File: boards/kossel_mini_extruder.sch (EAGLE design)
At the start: 31 parts

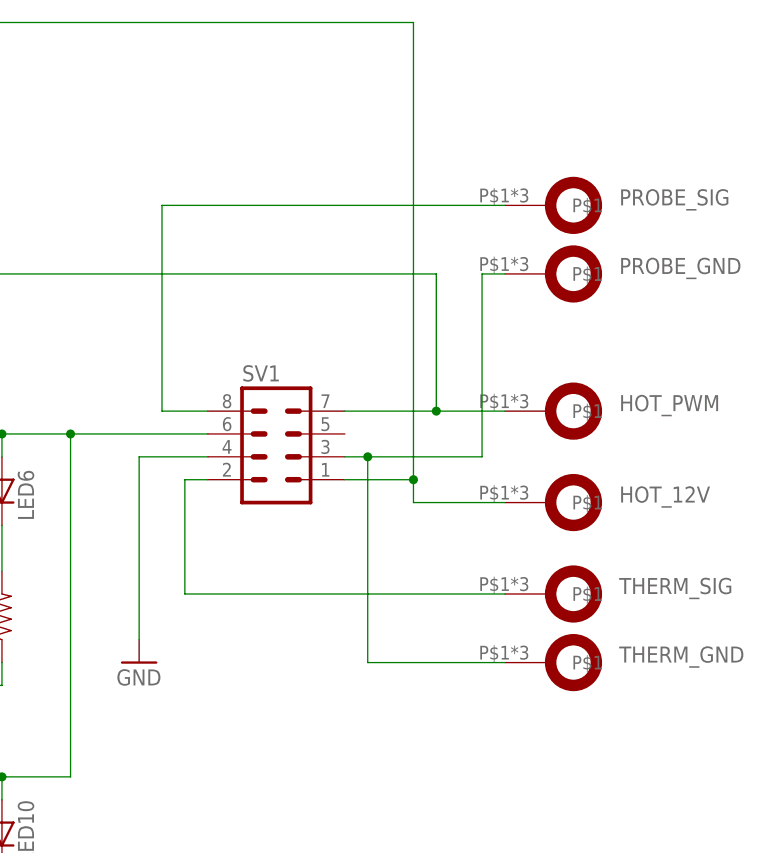
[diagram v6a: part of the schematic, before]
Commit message: started rev of end effector board
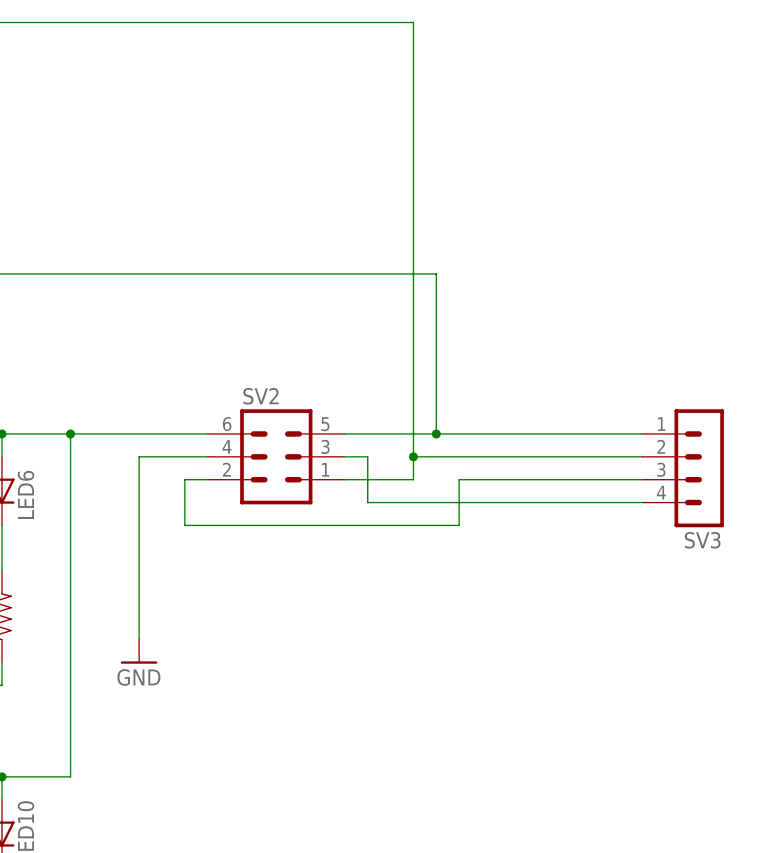
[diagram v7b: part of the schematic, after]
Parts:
- removed HOT_12V, HOT_PWM, PROBE_GND, PROBE_SIG, THERM_GND, THERM_SIG: LUG3-X, OBKP_Effector_PCB:LUG3-X
- removed SV1: (no value), con-lstb:MA04-2
- added SV2: (no value), con-lstb:MA03-2
- added SV3: (no value), con-lstb:MA04-1
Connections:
- removed net N$10: SV1.2, THERM_SIG.P$1
- removed net N$20: PROBE_SIG.P$1, SV1.8
- removed net N$7: HOT_PWM.P$1, R11.1, R12.1, R13.1, SV1.7
- removed net N$8: PROBE_GND.P$1, SV1.3, THERM_GND.P$1
- removed net VCC1: HOT_12V.P$1, LED11.A, LED12.A, LED13.A, SV1.1
- new net HOT_12V: R11.1, R12.1, R13.1, SV2.5, SV3.1
- new net HOT_SIG: LED11.A, LED12.A, LED13.A, SV2.1, SV3.2
- new net THERM_GND: SV2.3, SV3.4
- new net THERM_SIG: SV2.2, SV3.3
- net GND: now also SV2.4; no longer SV1.4
- net VCC: now also SV2.6; no longer SV1.6
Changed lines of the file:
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@@
 <part name="R5" library="SparkFun-Passives" deviceset="RESISTOR" device="0805-RES"/>
 <part name="R6" library="SparkFun-Passives" deviceset="RESISTOR" device="0805-RES"/>
-<part name="HOT_PWM" library="OBKP_Effector_PCB" deviceset="LUG" device="3-X"/>
-<part name="THERM_SIG" library="OBKP_Effector_PCB" deviceset="LUG" device="3-X"/>
-<part name="THERM_GND" library="OBKP_Effector_PCB" deviceset="LUG" device="3-X"/>
 <part name="GND1" library="SparkFun-Aesthetics" deviceset="GND" device=""/>
 <part name="GND3" library="SparkFun-Aesthetics" deviceset="GND" device=""/>
@@
 <part name="R10" library="SparkFun-Passives" deviceset="RESISTOR" device="0805-RES"/>
 <part name="GND5" library="SparkFun-Aesthetics" deviceset="GND" device=""/>
-<part name="HOT_12V" library="OBKP_Effector_PCB" deviceset="LUG" device="3-X"/>
-<part name="PROBE_GND" library="OBKP_Effector_PCB" deviceset="LUG" device="3-X"/>
-<part name="PROBE_SIG" library="OBKP_Effector_PCB" deviceset="LUG" device="3-X"/>
-<part name="SV1" library="con-lstb" deviceset="MA04-2" device=""/>
 <part name="LED11" library="SparkFun-LED" deviceset="LED" device="0805"/>
 <part name="LED12" library="SparkFun-LED" deviceset="LED" device="0805"/>
@@
 <part name="R12" library="SparkFun-Passives" deviceset="RESISTOR" device="0805-RES"/>
 <part name="R13" library="SparkFun-Passives" deviceset="RESISTOR" device="0805-RES"/>
+<part name="SV2" library="con-lstb" deviceset="MA03-2" device=""/>
+<part name="SV3" library="con-lstb" deviceset="MA04-1" device=""/>
 </parts>
 <sheets>
@@
 <instance part="R5" gate="G$1" x="-2.54" y="55.88" rot="R90"/>
 <instance part="R6" gate="G$1" x="7.62" y="55.88" rot="R90"/>
-<instance part="HOT_PWM" gate="G$1" x="63.5" y="78.74" smashed="yes" rot="R270">
-<attribute name="NAME" x="76.2" y="78.74" size="1.778" layer="95"/>
-</instance>
-<instance part="THERM_SIG" gate="G$1" x="63.5" y="58.42" smashed="yes" rot="R270">
-<attribute name="NAME" x="76.2" y="58.42" size="1.778" layer="95"/>
-</instance>
-<instance part="THERM_GND" gate="G$1" x="63.5" y="50.8" smashed="yes" rot="R270">
-<attribute name="NAME" x="76.2" y="50.8" size="1.778" layer="95"/>
-</instance>
 <instance part="GND1" gate="1" x="22.86" y="50.8"/>
 <instance part="GND3" gate="1" x="-17.78" y="43.18"/>
@@
 <instance part="R10" gate="G$1" x="7.62" y="17.78" rot="R90"/>
 <instance part="GND5" gate="1" x="-17.78" y="5.08"/>
-<instance part="HOT_12V" gate="G$1" x="63.5" y="68.58" smashed="yes" rot="R270">
-<attribute name="NAME" x="76.2" y="68.58" size="1.778" layer="95"/>
-</instance>
-<instance part="PROBE_GND" gate="G$1" x="63.5" y="93.98" smashed="yes" rot="R270">
-<attribute name="NAME" x="76.2" y="93.98" size="1.778" layer="95"/>
-</instance>
-<instance part="PROBE_SIG" gate="G$1" x="63.5" y="101.6" smashed="yes" rot="R270">
-<attribute name="NAME" x="76.2" y="101.6" size="1.778" layer="95"/>
-</instance>
-<instance part="SV1" gate="G$1" x="38.1" y="76.2"/>
 <instance part="LED11" gate="G$1" x="-22.86" y="116.84"/>
 <instance part="LED12" gate="G$1" x="-12.7" y="116.84"/>
@@
 <instance part="R12" gate="G$1" x="-12.7" y="101.6" rot="R90"/>
 <instance part="R13" gate="G$1" x="-2.54" y="101.6" rot="R90"/>
+<instance part="SV2" gate="1" x="38.1" y="73.66"/>
+<instance part="SV3" gate="1" x="86.36" y="71.12" rot="R180"/>
 </instances>
 <busses>
@@
 </segment>
 <segment>
-<pinref part="SV1" gate="G$1" pin="4"/>
-<wire x1="22.86" y1="73.66" x2="30.48" y2="73.66" width="0.1524" layer="91"/>
 <pinref part="GND1" gate="1" pin="GND"/>
 <wire x1="22.86" y1="53.34" x2="22.86" y2="73.66" width="0.1524" layer="91"/>
+<pinref part="SV2" gate="1" pin="4"/>
+<wire x1="22.86" y1="73.66" x2="30.48" y2="73.66" width="0.1524" layer="91"/>
 </segment>
 </net>
@@
 <junction x="7.62" y="76.2"/>
 <wire x1="15.24" y1="38.1" x2="15.24" y2="76.2" width="0.1524" layer="91"/>
+<junction x="15.24" y="76.2"/>
+<pinref part="SV2" gate="1" pin="6"/>
 <wire x1="15.24" y1="76.2" x2="30.48" y2="76.2" width="0.1524" layer="91"/>
-<junction x="15.24" y="76.2"/>
-<pinref part="SV1" gate="G$1" pin="6"/>
-</segment>
-</net>
-<net name="N$8" class="0">
-<segment>
-<pinref part="THERM_GND" gate="G$1" pin="P$1"/>
-<wire x1="63.5" y1="50.8" x2="48.26" y2="50.8" width="0.1524" layer="91"/>
-<wire x1="48.26" y1="50.8" x2="48.26" y2="73.66" width="0.1524" layer="91"/>
-<wire x1="48.26" y1="73.66" x2="60.96" y2="73.66" width="0.1524" layer="91"/>
-<pinref part="PROBE_GND" gate="G$1" pin="P$1"/>
-<wire x1="63.5" y1="93.98" x2="60.96" y2="93.98" width="0.1524" layer="91"/>
-<wire x1="60.96" y1="73.66" x2="60.96" y2="93.98" width="0.1524" layer="91"/>
-<pinref part="SV1" gate="G$1" pin="3"/>
+</segment>
+</net>
+<net name="THERM_GND" class="0">
+<segment>
+<pinref part="SV2" gate="1" pin="3"/>
 <wire x1="45.72" y1="73.66" x2="48.26" y2="73.66" width="0.1524" layer="91"/>
-<junction x="48.26" y="73.66"/>
+<wire x1="48.26" y1="73.66" x2="48.26" y2="68.58" width="0.1524" layer="91"/>
+<pinref part="SV3" gate="1" pin="4"/>
+<wire x1="48.26" y1="68.58" x2="78.74" y2="68.58" width="0.1524" layer="91"/>
 </segment>
 </net>
@@
 </segment>
 </net>
-<net name="VCC1" class="0">
+<net name="HOT_SIG" class="0">
 <segment>
 <pinref part="LED11" gate="G$1" pin="A"/>
@@
 <wire x1="53.34" y1="121.92" x2="-2.54" y2="121.92" width="0.1524" layer="91"/>
 <junction x="-2.54" y="121.92"/>
-<pinref part="HOT_12V" gate="G$1" pin="P$1"/>
-<wire x1="53.34" y1="68.58" x2="63.5" y2="68.58" width="0.1524" layer="91"/>
-<wire x1="53.34" y1="68.58" x2="53.34" y2="71.12" width="0.1524" layer="91"/>
-<pinref part="SV1" gate="G$1" pin="1"/>
+<wire x1="53.34" y1="121.92" x2="53.34" y2="73.66" width="0.1524" layer="91"/>
+<pinref part="SV2" gate="1" pin="1"/>
+<wire x1="53.34" y1="73.66" x2="53.34" y2="71.12" width="0.1524" layer="91"/>
 <wire x1="45.72" y1="71.12" x2="53.34" y2="71.12" width="0.1524" layer="91"/>
-<wire x1="53.34" y1="121.92" x2="53.34" y2="71.12" width="0.1524" layer="91"/>
-<junction x="53.34" y="71.12"/>
-</segment>
-</net>
-<net name="N$20" class="0">
-<segment>
-<pinref part="PROBE_SIG" gate="G$1" pin="P$1"/>
-<wire x1="25.4" y1="101.6" x2="63.5" y2="101.6" width="0.1524" layer="91"/>
-<wire x1="25.4" y1="101.6" x2="25.4" y2="78.74" width="0.1524" layer="91"/>
-<pinref part="SV1" gate="G$1" pin="8"/>
-<wire x1="25.4" y1="78.74" x2="30.48" y2="78.74" width="0.1524" layer="91"/>
-</segment>
-</net>
-<net name="N$7" class="0">
+<junction x="53.34" y="73.66"/>
+<pinref part="SV3" gate="1" pin="2"/>
+<wire x1="53.34" y1="73.66" x2="78.74" y2="73.66" width="0.1524" layer="91"/>
+</segment>
+</net>
+<net name="HOT_12V" class="0">
 <segment>
 <pinref part="R11" gate="G$1" pin="1"/>
@@
 <wire x1="-12.7" y1="96.52" x2="-12.7" y2="93.98" width="0.1524" layer="91"/>
 <junction x="-12.7" y="93.98"/>
-<pinref part="HOT_PWM" gate="G$1" pin="P$1"/>
-<wire x1="45.72" y1="78.74" x2="55.88" y2="78.74" width="0.1524" layer="91"/>
-<pinref part="SV1" gate="G$1" pin="7"/>
-<wire x1="55.88" y1="78.74" x2="63.5" y2="78.74" width="0.1524" layer="91"/>
 <wire x1="-2.54" y1="93.98" x2="55.88" y2="93.98" width="0.1524" layer="91"/>
-<wire x1="55.88" y1="93.98" x2="55.88" y2="78.74" width="0.1524" layer="91"/>
-<junction x="55.88" y="78.74"/>
+<wire x1="55.88" y1="93.98" x2="55.88" y2="76.2" width="0.1524" layer="91"/>
 <junction x="-2.54" y="93.98"/>
-</segment>
-</net>
-<net name="N$10" class="0">
-<segment>
-<pinref part="SV1" gate="G$1" pin="2"/>
-<wire x1="30.48" y1="71.12" x2="27.94" y2="71.12" width="0.1524" layer="91"/>
-<wire x1="27.94" y1="71.12" x2="27.94" y2="58.42" width="0.1524" layer="91"/>
-<pinref part="THERM_SIG" gate="G$1" pin="P$1"/>
-<wire x1="27.94" y1="58.42" x2="63.5" y2="58.42" width="0.1524" layer="91"/>
-</segment>
-</net>
+<pinref part="SV2" gate="1" pin="5"/>
+<wire x1="55.88" y1="76.2" x2="45.72" y2="76.2" width="0.1524" layer="91"/>
+<junction x="55.88" y="76.2"/>
+<pinref part="SV3" gate="1" pin="1"/>
+<wire x1="55.88" y1="76.2" x2="78.74" y2="76.2" width="0.1524" layer="91"/>
+</segment>
+</net>
+<net name="THERM_SIG" class="0">
+<segment>
+<pinref part="SV2" gate="1" pin="2"/>
+<wire x1="27.94" y1="71.12" x2="30.48" y2="71.12" width="0.1524" layer="91"/>
+<wire x1="27.94" y1="71.12" x2="27.94" y2="66.04" width="0.1524" layer="91"/>
+<wire x1="27.94" y1="66.04" x2="58.42" y2="66.04" width="0.1524" layer="91"/>
+<wire x1="58.42" y1="66.04" x2="58.42" y2="71.12" width="0.1524" layer="91"/>
+<pinref part="SV3" gate="1" pin="3"/>
+<wire x1="58.42" y1="71.12" x2="78.74" y2="71.12" width="0.1524" layer="91"/>
+</segment>
+</net>
